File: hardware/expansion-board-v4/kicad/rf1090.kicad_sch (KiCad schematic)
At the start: 50 parts, among them J6 U.FL_1090_EXT(经尾线转SMA), J7 U.FL_IFA_TEST(π后调试口), Q3 AO3401A, U11 QPL9547TR7, U12 BGA2817, U13 AD8319ACPZ-R7(主), U14 AD8313ARMZ(备,二选一), U15 TLV3501(TOKMAS), U16 XA17-G4K(或AS179-92LF)

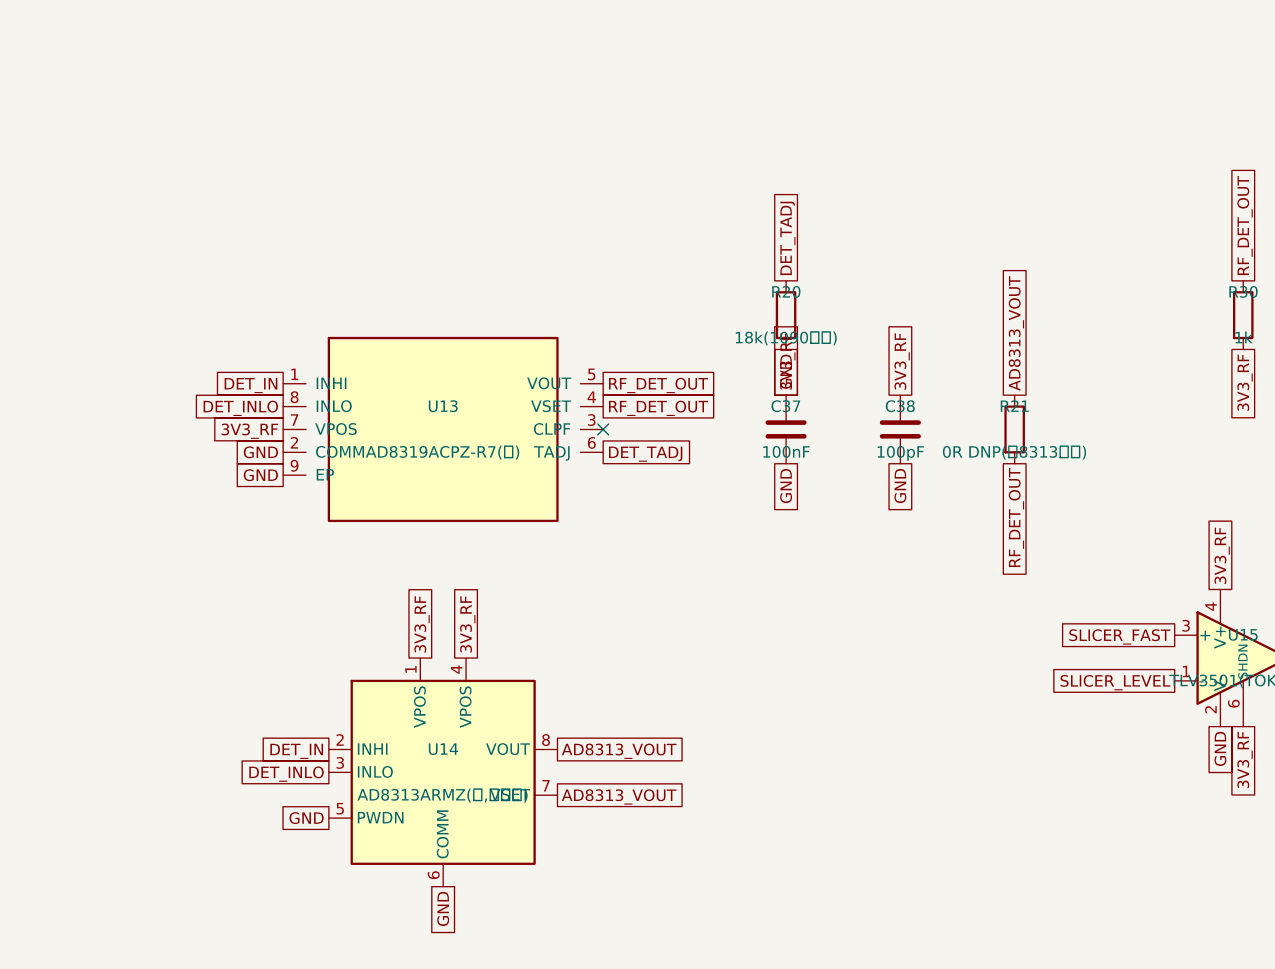
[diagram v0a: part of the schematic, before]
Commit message: change(v4): 检波器定为 AD8313，删除 AD8319(U13) 与 R20
## 决策依据

2026-08-01 选 AD8319 纯粹是采购逼的：当时 AD8313 立创 ¥71.37 且现货仅 5，
AD8319 ¥21.9 库存 6441。技术上 AD8319 是更差的那个：
    动态范围    AD8313 70dB   vs  AD8319 ~40dB
    预估灵敏度  ≈-105dBm      vs  -95~-100dBm
ADSBee 原设计用的也是 AD8313，所以当时留了双封装位准备投板 A/B。

现在用户在淘宝实际买到 AD8313 ¥4.8、AD8319 反而 ¥6.8，价格依据整个反转，
A/B 对比失去意义，直接定 AD8313。

顺带解决两个问题：
- U13↔U14 共享 DET_IN/DET_INLO 相隔 8.50mm，不贴的那颗是残桩，1090MHz 上影响匹配
- AD8319 是 LFCSP-8 带裸焊盘（ASSEMBLY 标 ★★★ 只能热风）；AD8313 是 MSOP-8 烙铁可焊

⚠️ 采购风险仍在：询价记录里淘宝 AD8313 低云价 1.5~5.5 被判「全是仿标」，
¥4.8 正落在该区间。上电必须验 VOUT 斜率是否为 ADI 手册的 ~18mV/dB。

## 改动

原理图源 sheet_rf1090.py：删 U13、删 R20（DET_TADJ 是 AD8319 独有的温补脚），
U14 值 "AD8313ARMZ(备,二选一)" → "AD8313ARMZ"，R21 "0R DNP(选8313时贴)" → "0R"（必贴，
AD8313_VOUT→RF_DET_OUT 现在是唯一通路）。重生成 rf1090.kicad_sch（48 符号）。

PCB：删 U13/R20 两个封装，176 → 174 件。重生成 build/netlist.xml（170 元件）。

生成脚本连带更新 7 个：gen_checklist / gen_assembly / gen_bom / gen_bom_smt /
gen_bom_xlsx / fanout_channel / ep_targets——U14 从「默认不贴」改为必贴。
gen_checklist.py 的计数断言原来把 U14 同时算进「要贴」和「不贴」，分类规则一改
就重复计数顶穿断言，一并修正。

## 验收

parity 0（原理图与 PCB 同步）、DRC 8 条 0 error、未连接 298 → 292、
IFA 走廊 5 项测试通过。C34→检波器 13.77 → 7.32mm。

遗留（均为用户手工布局，非本次引入）：
- FL1 ↔ C31 courtyard 重叠（用户在 78abd2a 后挪 C31 3.3mm 造成）
- C35 → U14 10.20mm、R21 → U14 15.40mm，需跟着 U14 重排
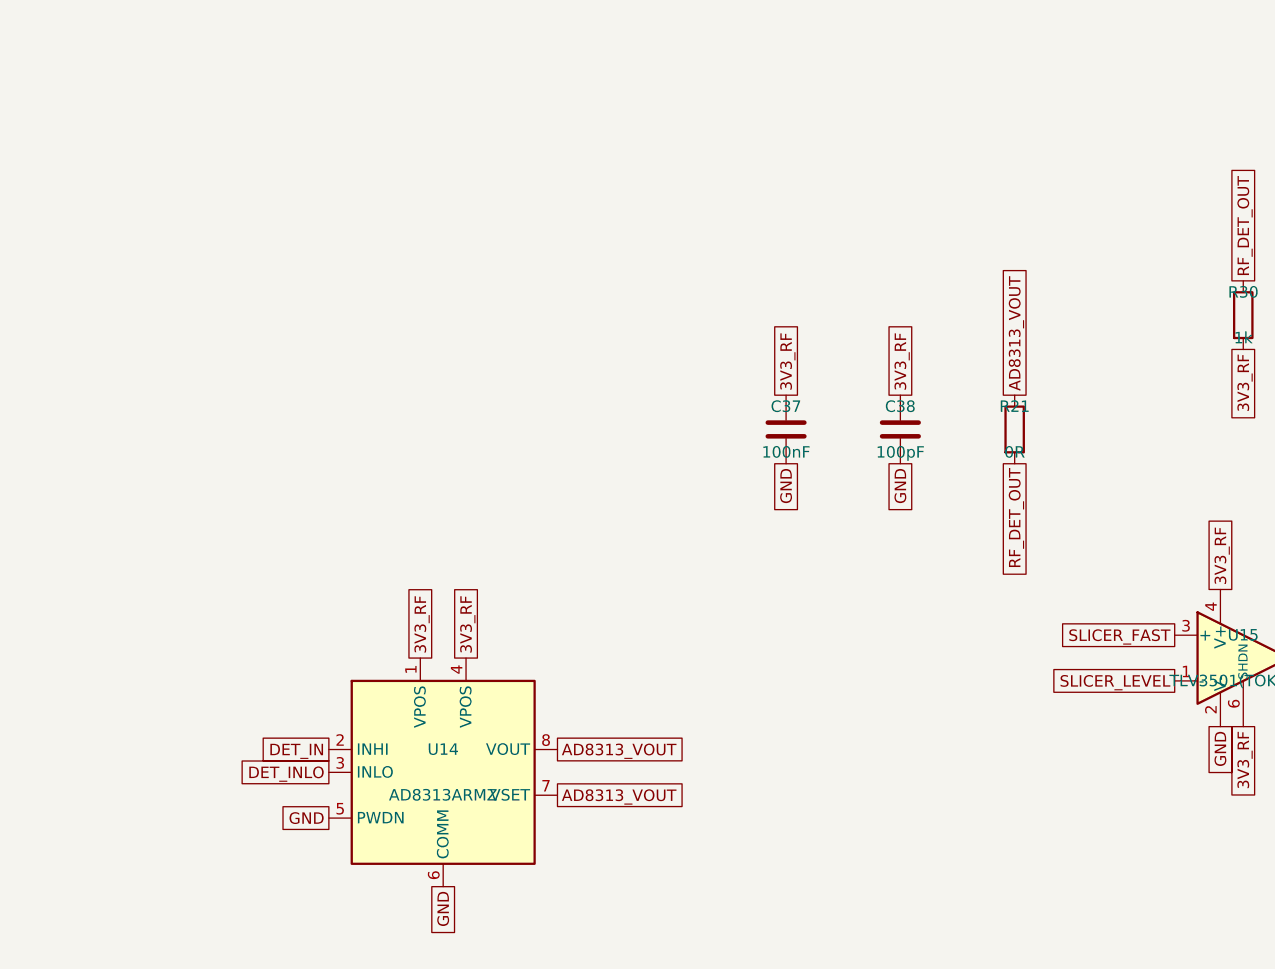
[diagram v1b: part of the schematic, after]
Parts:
- removed R20: 18k(1090实调), Resistor_SMD:R_0603_1608Metric, symbol Device:R
- removed U13: AD8319ACPZ-R7(主), expansion-board-v4:AD8319_LFCSP-8-EP, symbol expansion-board-v4:AD8319
- R21: value 0R DNP(选8313时贴) -> 0R
- U14: value AD8313ARMZ(备,二选一) -> AD8313ARMZ
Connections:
- no-connect marks 1 -> 0
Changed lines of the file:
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@@
 				(hide yes))
+		)
+		(pin "A"
 		)
 		(pin "B"
 		)
-		(pin "A"
-		)
 		(pin "C"
 		)
+		(pin "D"
+		)
 		(pin "E"
-		)
-		(pin "D"
 		)
 		(pin "F"
@@
 				(hide yes))
 		)
+		(pin "A"
+		)
 		(pin "B"
 		)
-		(pin "A"
-		)
 		(pin "C"
 		)
+		(pin "D"
+		)
 		(pin "E"
-		)
-		(pin "D"
 		)
 		(pin "F"
@@
 	)
 	(symbol
-		(lib_id "expansion-board-v4:AD8319")
-		(at 63.5 152.4 0)
-		(unit 1)
-		(exclude_from_sim no)
-		(in_bom yes)
-		(on_board yes)
-		(dnp no)
-		(property "Reference" "U13"
-			(at 63.5 149.86 0)
-			(effects (font (size 1.27 1.27)))
-		)
-		(property "Value" "AD8319ACPZ-R7(主)"
-			(at 63.5 154.94 0)
-			(effects (font (size 1.27 1.27)))
-		)
-		(property "Footprint" "expansion-board-v4:AD8319_LFCSP-8-EP"
-			(at 63.5 157.48 0)
-			(effects (font (size 1.27 1.27))
-				(hide yes))
-		)
-		(property "Datasheet" "~"
-			(at 63.5 160.02 0)
-			(effects (font (size 1.27 1.27))
-				(hide yes))
-		)
-		(pin "1"
-		)
-		(pin "8"
-		)
-		(pin "7"
-		)
-		(pin "2"
-		)
-		(pin "9"
-		)
-		(pin "5"
-		)
-		(pin "4"
-		)
-		(pin "3"
-		)
-		(pin "6"
-		)
-		(instances
-			(project "expansion-board-v4"
-				(path "/10000000-0000-4000-8000-000000000001/20000000-0000-4000-8000-000000000003"
-					(reference "U13")
-					(unit 1)
-				)
-			)
-		)
-	)
-	(global_label "DET_IN"
-		(shape passive)
-		(at 45.72 147.32 180)
-		(effects (font (size 1.27 1.27)) (justify right))
-	)
-	(global_label "DET_INLO"
-		(shape passive)
-		(at 45.72 149.86 180)
-		(effects (font (size 1.27 1.27)) (justify right))
-	)
-	(global_label "3V3_RF"
-		(shape passive)
-		(at 45.72 152.4 180)
-		(effects (font (size 1.27 1.27)) (justify right))
-	)
-	(global_label "GND"
-		(shape passive)
-		(at 45.72 154.94 180)
-		(effects (font (size 1.27 1.27)) (justify right))
-	)
-	(global_label "GND"
-		(shape passive)
-		(at 45.72 157.48 180)
-		(effects (font (size 1.27 1.27)) (justify right))
-	)
-	(global_label "RF_DET_OUT"
-		(shape passive)
-		(at 81.28 147.32 0)
-		(effects (font (size 1.27 1.27)) (justify left))
-	)
-	(global_label "RF_DET_OUT"
-		(shape passive)
-		(at 81.28 149.86 0)
-		(effects (font (size 1.27 1.27)) (justify left))
-	)
-	(no_connect
-		(at 81.28 152.4)
-	)
-	(global_label "DET_TADJ"
-		(shape passive)
-		(at 81.28 154.94 0)
-		(effects (font (size 1.27 1.27)) (justify left))
-	)
-	(symbol
-		(lib_id "Device:R")
-		(at 101.6 139.7 0)
-		(unit 1)
-		(exclude_from_sim no)
-		(in_bom yes)
-		(on_board yes)
-		(dnp no)
-		(property "Reference" "R20"
-			(at 101.6 137.16 0)
-			(effects (font (size 1.27 1.27)))
-		)
-		(property "Value" "18k(1090实调)"
-			(at 101.6 142.24 0)
-			(effects (font (size 1.27 1.27)))
-		)
-		(property "Footprint" "Resistor_SMD:R_0603_1608Metric"
-			(at 101.6 144.78 0)
-			(effects (font (size 1.27 1.27))
-				(hide yes))
-		)
-		(property "Datasheet" "~"
-			(at 101.6 147.32 0)
-			(effects (font (size 1.27 1.27))
-				(hide yes))
-		)
-		(pin "1"
-		)
-		(pin "2"
-		)
-		(instances
-			(project "expansion-board-v4"
-				(path "/10000000-0000-4000-8000-000000000001/20000000-0000-4000-8000-000000000003"
-					(reference "R20")
-					(unit 1)
-				)
-			)
-		)
-	)
-	(global_label "DET_TADJ"
-		(shape passive)
-		(at 101.6 135.89 270)
-		(effects (font (size 1.27 1.27)) (justify left))
-	)
-	(global_label "GND"
-		(shape passive)
-		(at 101.6 143.51 90)
-		(effects (font (size 1.27 1.27)) (justify right))
-	)
-	(symbol
 		(lib_id "RF_Amplifier:AD8313xRM")
 		(at 63.5 190.5 0)
@@
 			(effects (font (size 1.27 1.27)))
 		)
-		(property "Value" "AD8313ARMZ(备,二选一)"
+		(property "Value" "AD8313ARMZ"
 			(at 63.5 193.04 0)
 			(effects (font (size 1.27 1.27)))
@@
 			(effects (font (size 1.27 1.27)))
 		)
-		(property "Value" "0R DNP(选8313时贴)"
+		(property "Value" "0R"
 			(at 127 154.94 0)
 			(effects (font (size 1.27 1.27)))

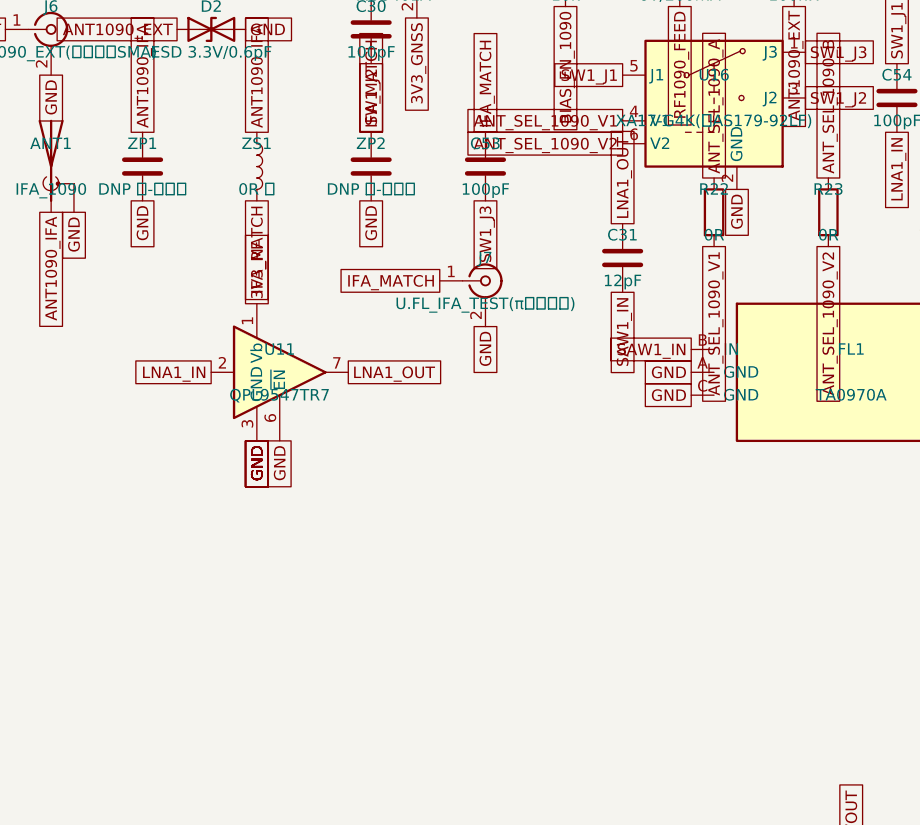
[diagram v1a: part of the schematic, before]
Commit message: fix(v4): correct RF and power networks for V4.2
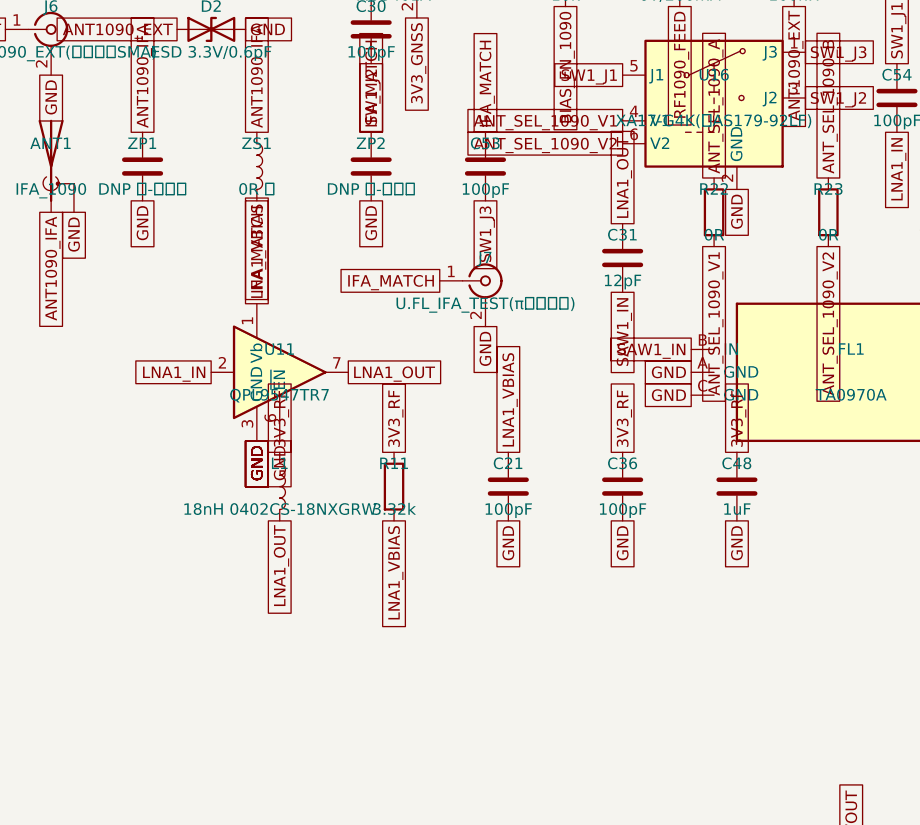
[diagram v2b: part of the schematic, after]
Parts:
- added C21, C36: 100pF, Capacitor_SMD:C_0402_1005Metric, symbol Device:C
- added C48: 1uF, Capacitor_SMD:C_0402_1005Metric, symbol Device:C
- added L1: 18nH 0402CS-18NXGRW, Inductor_SMD:L_0402_1005Metric, symbol Device:L
- added R11: 3.32k, Resistor_SMD:R_0402_1005Metric, symbol Device:R
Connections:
- net 3V3_RF: now also C36.1, C48.1, L1.1, R11.1; no longer U11.1 (Vb)
- net GND: now also C21.2, C36.2, C48.2
- net LNA1_OUT: now also L1.2
- new net LNA1_VBIAS: C21.1, R11.2, U11.1 (Vb)

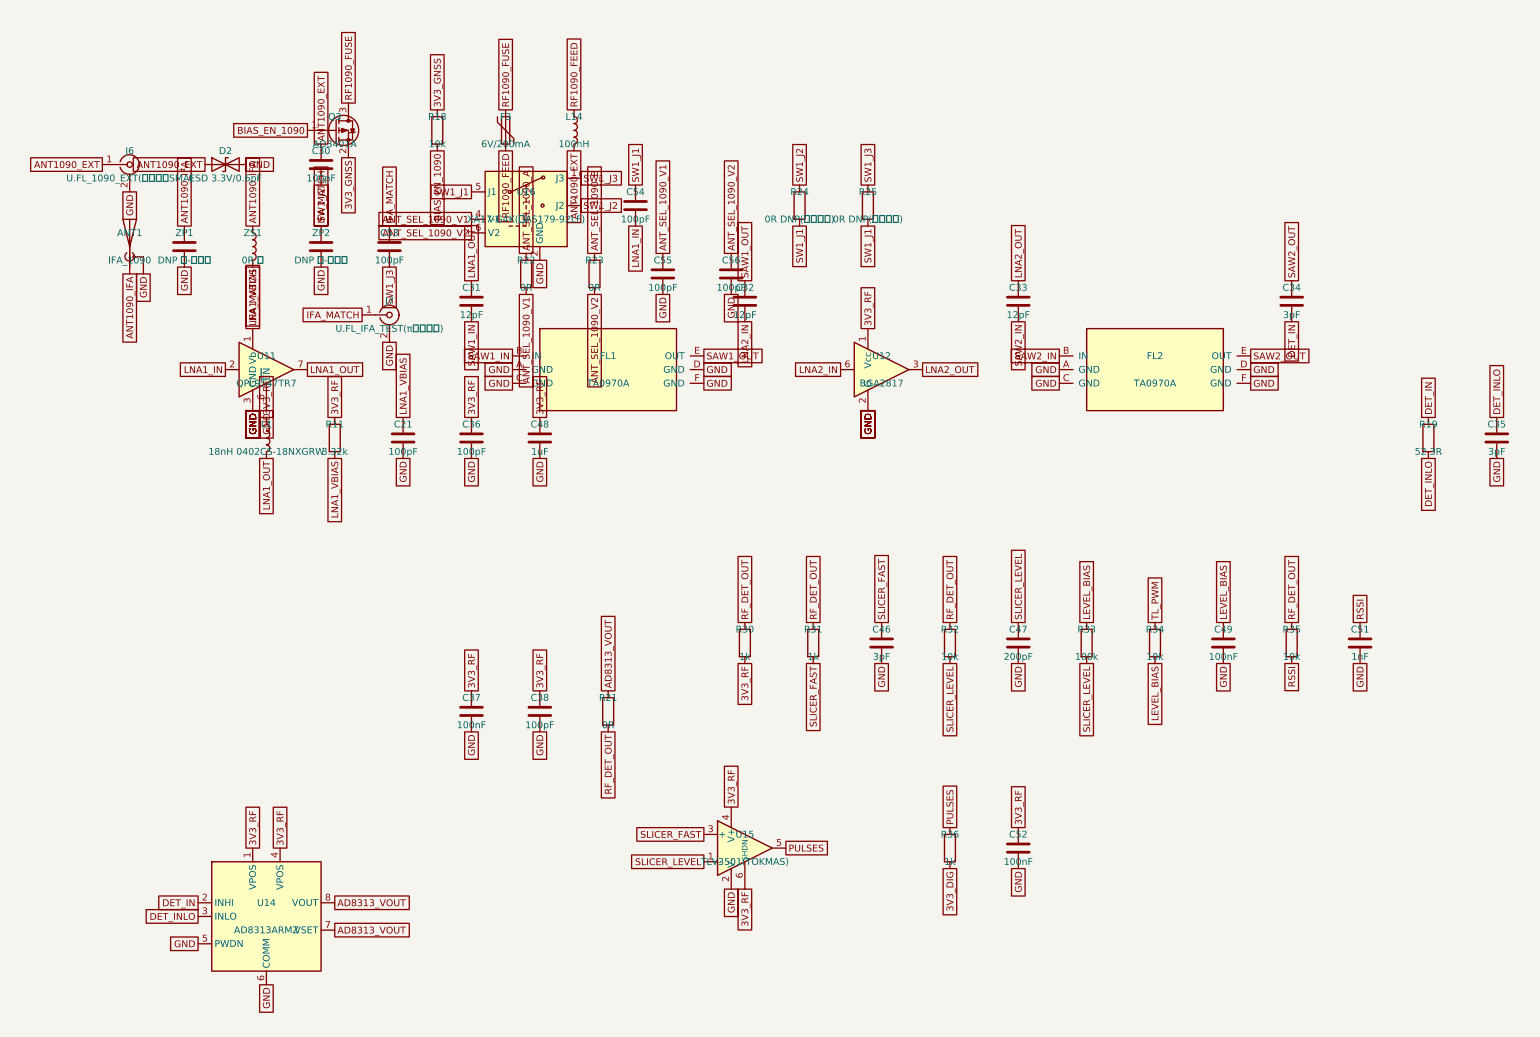
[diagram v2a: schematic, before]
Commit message: fix(v4): finalize V4.3 board after manual routing
罩哥手工完成全部布线后的定稿。DRC 0 violations / 0 unconnected。

板子本身:
- 1607 段走线 / 415 个过孔 / 207 个封装 / 15 个 zone
- RP_1V1 在 B.Cu 合并为单块 228.96mm2，四颗 RP_1V1 去耦落入其中
- C81 挪到 U12 旁 1.47mm(原 3.36mm)，脚下由「无铜」变为落在 B.Cu 的 3V3_RF 上
- U8.23(DVDD) 补一个 RP_1V1 过孔 @(85.798,72.600)，接入距离 1.63 -> 0.88mm
  落点在既有走线上，未改任何走线；与相邻 QFN 焊盘边缘间距 +0.312mm

原理图:
- rf1090 的 PWR_FLAG 由 #FLG05 改为 #FLG06。sheet_power.py 已占用 #FLG05,
  两页撞号会让网表导出报「批注错误」。改后网表 714 节点、网络归属零变化。

.kicad_pro 保留正式板原有的 FINE netclass(0.13mm, 用于 DEMOD0-3/RECOVERED_CLK/
SWCLK/SWDIO)。板上这 7 个网络实际都按 0.15mm 布线、FINE 处于闲置; 两份工程
文件下各跑一次 DRC 均为 0，且 drc_exclusions 都是空的。
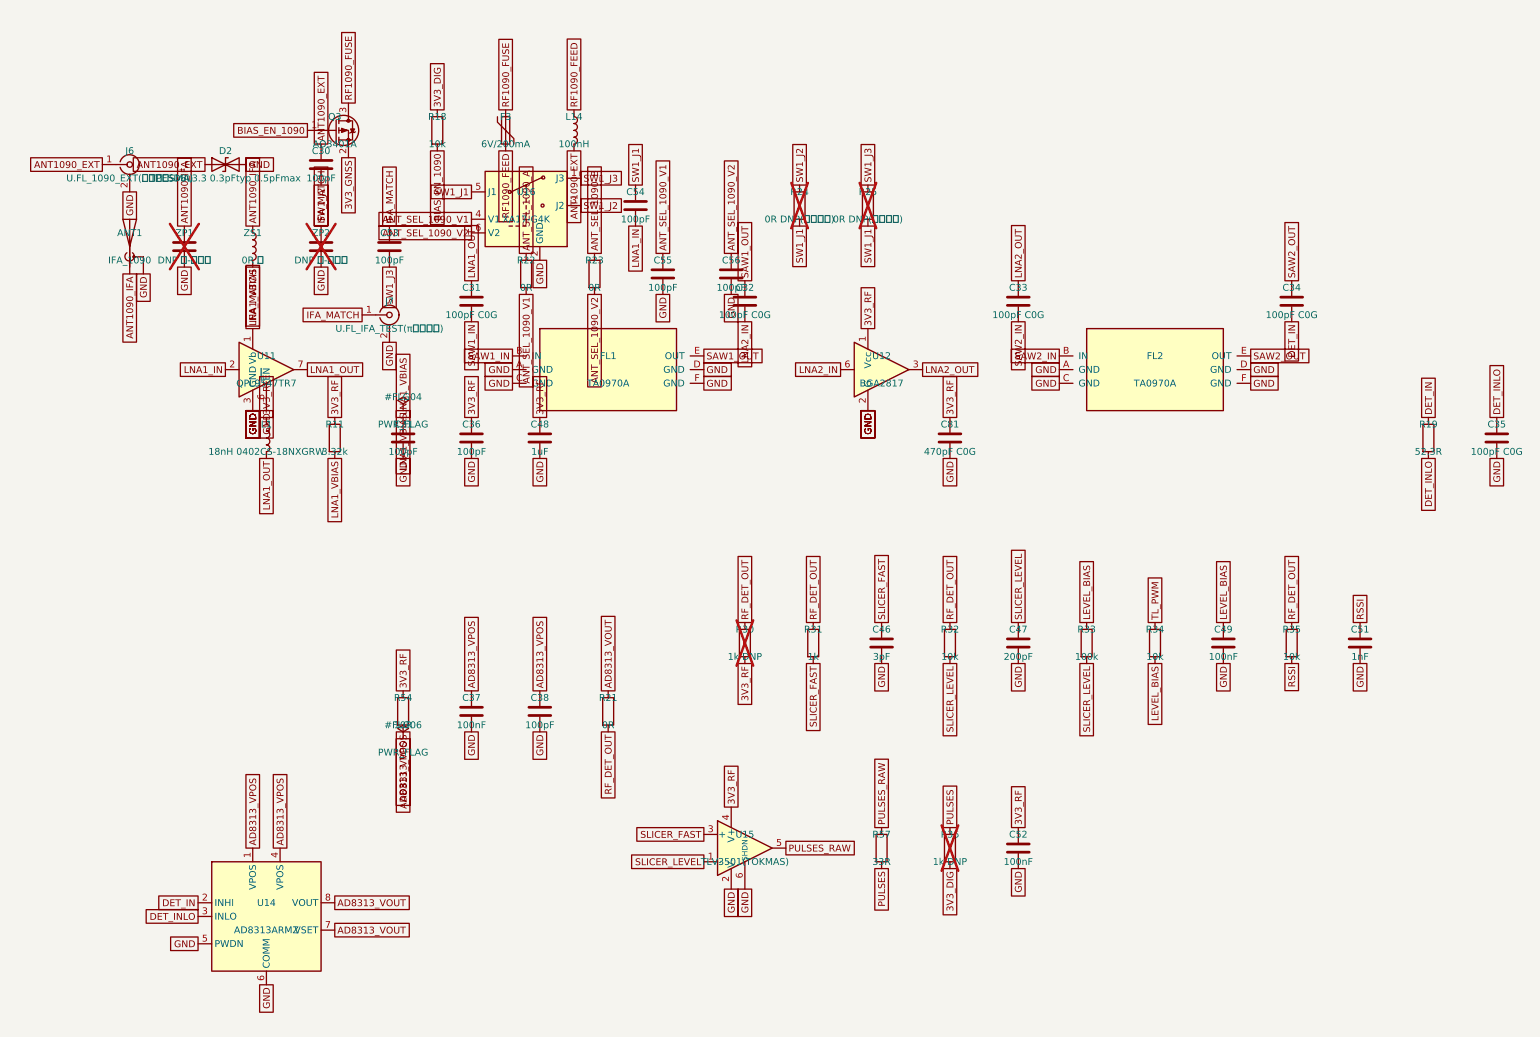
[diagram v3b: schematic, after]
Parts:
- added C81: 470pF C0G, Capacitor_SMD:C_0402_1005Metric, symbol Device:C
- added R54: 10R, Resistor_SMD:R_0402_1005Metric, symbol Device:R
- added R57: 33R, Resistor_SMD:R_0603_1608Metric, symbol Device:R
- C31, C32, C33: value 12pF -> 100pF C0G
- C34, C35: value 3pF -> 100pF C0G
- D2: value ESD 3.3V/0.6pF -> TPESD8L3.3 0.3pFtyp 0.5pFmax
- R24, R25, ZP1, ZP2: now not fitted
- R30, R36: value 1k -> 1k DNP; now not fitted
- U16: value XA17-G4K(或AS179-92LF) -> XA17-G4K
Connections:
- net 3V3_DIG: now also R18.1
- net 3V3_GNSS: no longer R18.1
- net 3V3_RF: now also C81.1, R54.1; no longer C37.1, C38.1, U14.1 (VPOS), U14.4 (VPOS), U15.6 (SHDN)
- net GND: now also U15.6 (SHDN), C81.2
- net PULSES: now also R57.2; no longer U15.5
- new net AD8313_VPOS: C37.1, C38.1, R54.2, U14.1 (VPOS), U14.4 (VPOS)
- new net PULSES_RAW: R57.1, U15.5
